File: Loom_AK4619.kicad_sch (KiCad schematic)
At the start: 129 parts, among them J1 Conn_01x40, J2 Conn_01x40, U1 AK4619VN, U101 HT75xx-1-SOT89, U2 AK4619VN, U3 OPA1679, U4 OPA1679, U5 OPA1679, U6 OPA1679

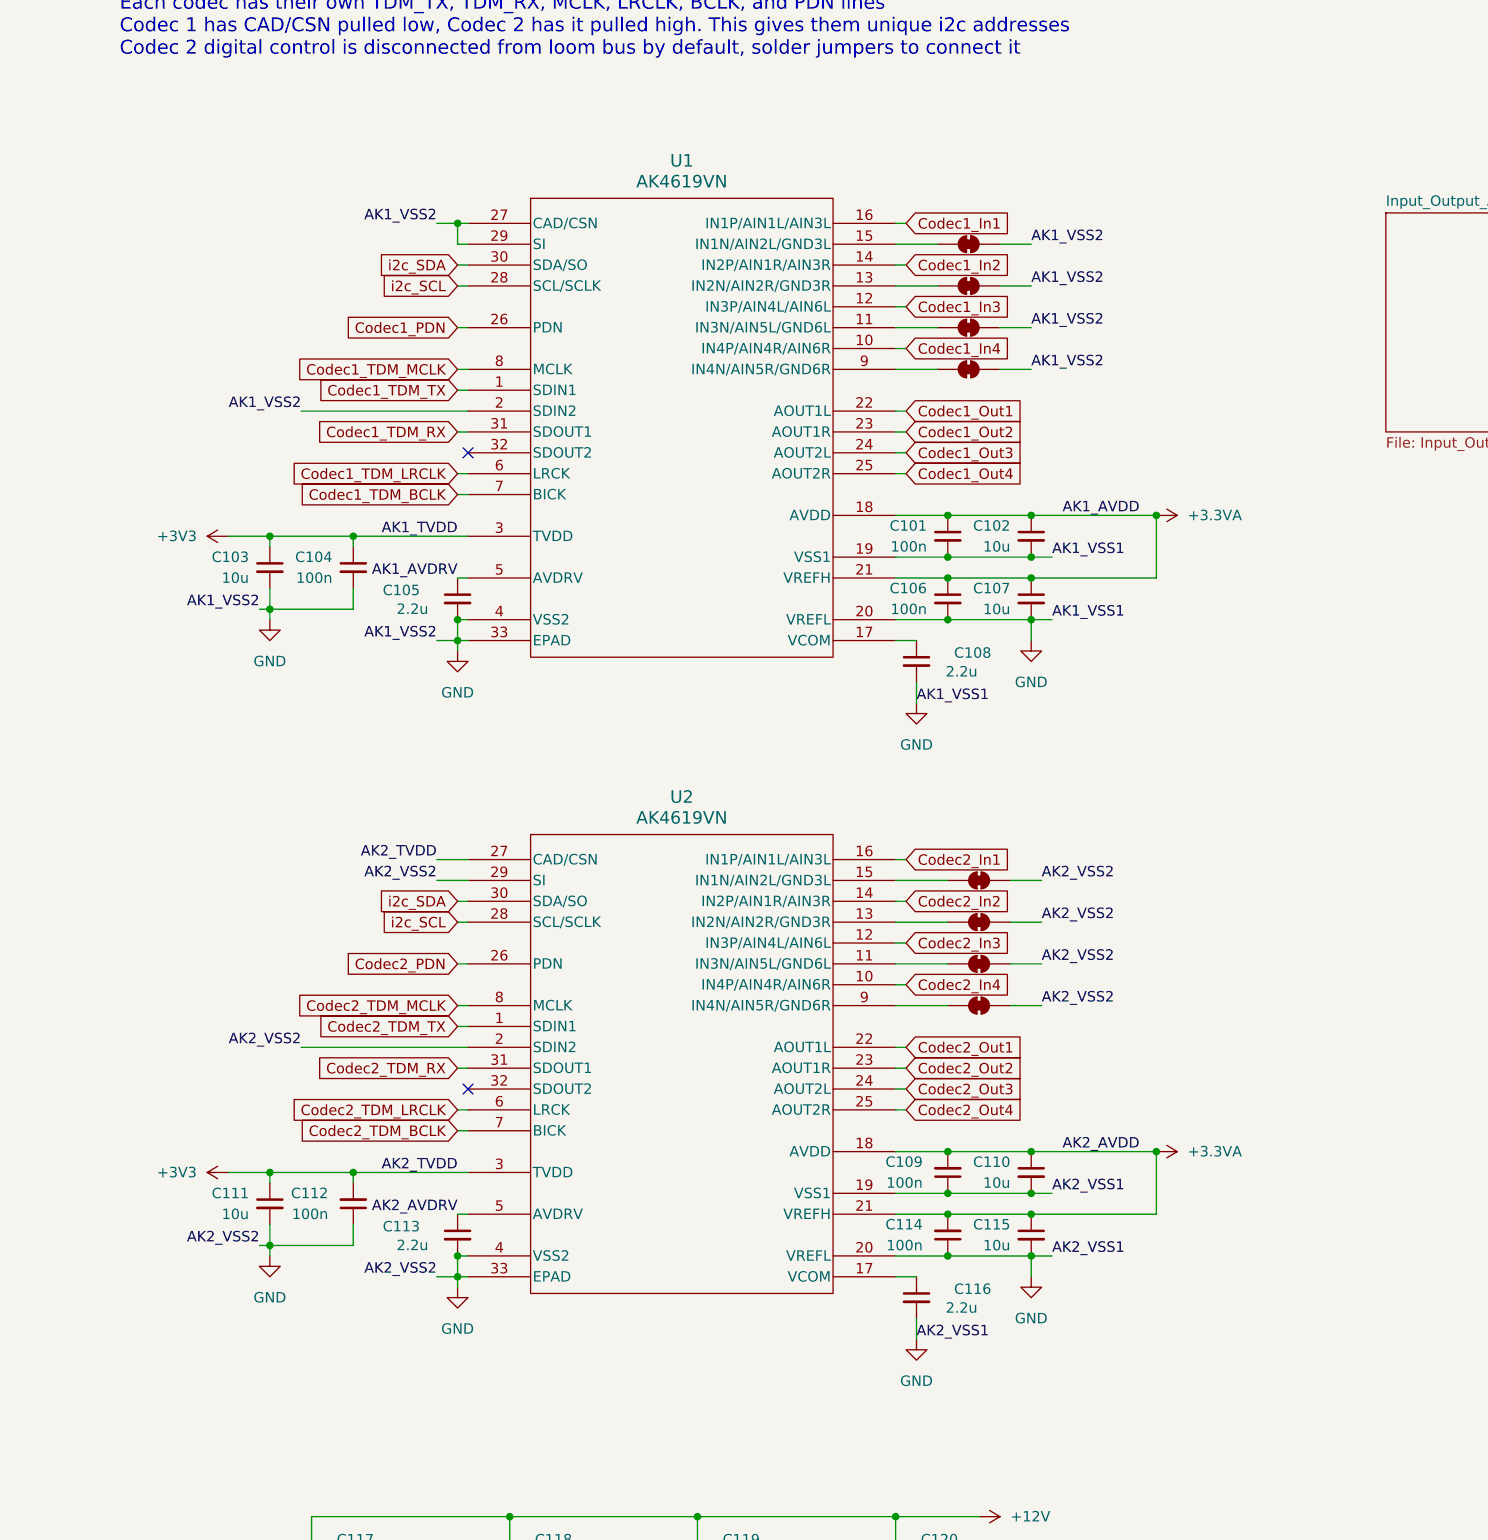
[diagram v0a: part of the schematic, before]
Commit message: Added 33R resistors to SDOUT
Added 33R resistors to SDOUT to decrease slew rate slightly to reduce radiated emissions.
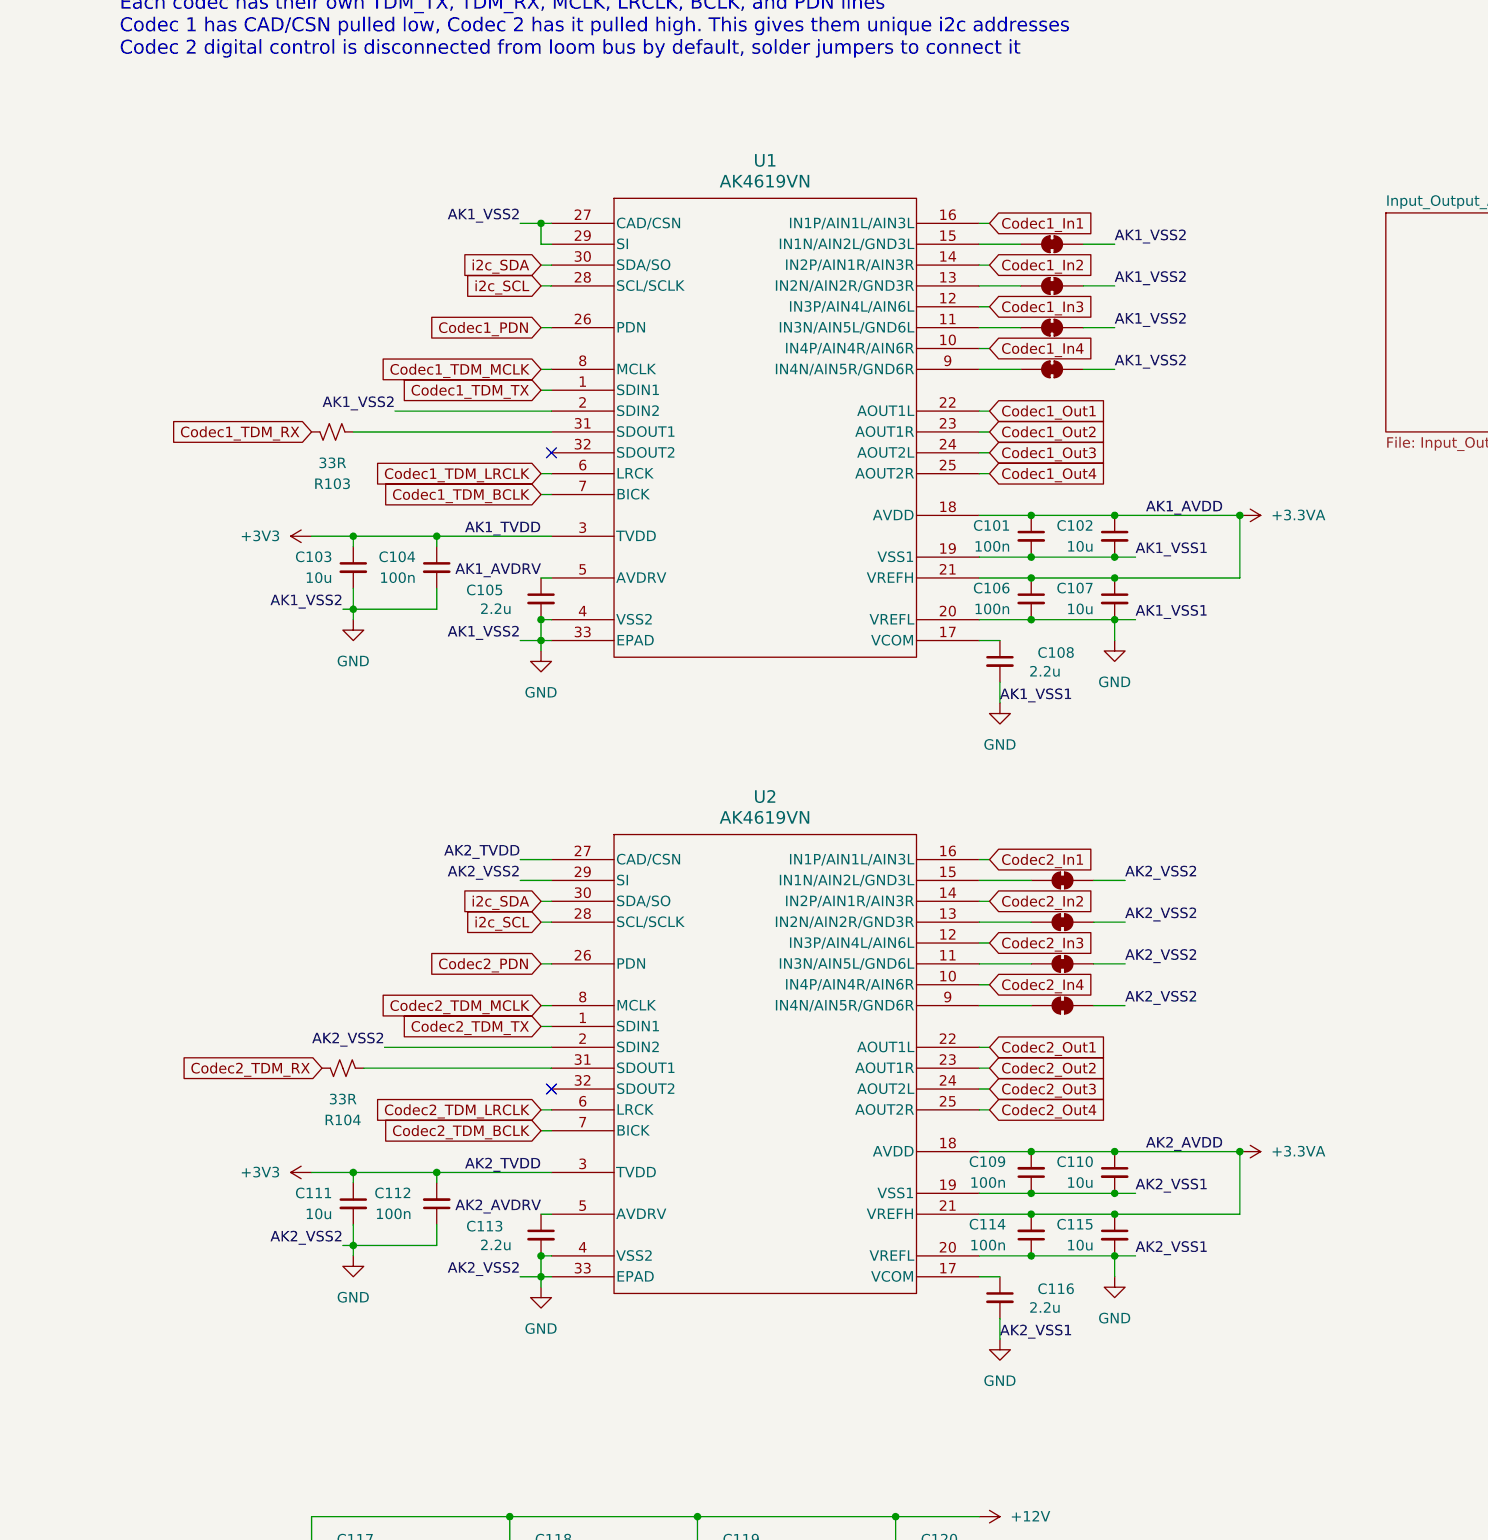
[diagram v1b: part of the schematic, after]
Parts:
- added R103, R104: 33R, winterbloom:R_0603_HandSolder, symbol Decapod_Devices:R_Small_US
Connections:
- net Codec1_TDM_RX: now also R103.1; no longer U1.31 (SDOUT1)
- net Codec2_TDM_RX: now also R104.1; no longer U2.31 (SDOUT1)
- new net: R104.2, U2.31 (SDOUT1)
- new net: R103.2, U1.31 (SDOUT1)
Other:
- moved on the sheet: C101, C102, C103, C104, C105, C106, C107, C108, C109, C110, C111, C112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

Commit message: Version 1 ready to order
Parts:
- R101: LCSC (none) -> C25804
- R102: LCSC (none) -> C23234
- R103, R104: LCSC (none) -> C23140
- U101: LCSC (none) -> C14289
- U3, U4, U5, U6: LCSC (none) -> C2057264
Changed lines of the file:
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@@
 	(label "AK1_VSS2"
 		(at 138.43 64.77 0)
-		(fields_autoplaced yes)
 		(effects
 			(font
@@
 	(label "AK2_VSS2"
 		(at 139.7 147.32 0)
-		(fields_autoplaced yes)
 		(effects
 			(font
@@
 	(label "AK1_VSS2"
 		(at 44.45 109.22 180)
-		(fields_autoplaced yes)
 		(effects
 			(font
@@
 	(label "AK2_TVDD"
 		(at 66.04 139.7 180)
-		(fields_autoplaced yes)
 		(effects
 			(font
@@
 	(label "AK2_VSS2"
 		(at 139.7 152.4 0)
-		(fields_autoplaced yes)
 		(effects
 			(font
@@
 	(label "AK1_VSS2"
 		(at 138.43 69.85 0)
-		(fields_autoplaced yes)
 		(effects
 			(font
@@
 	(label "AK1_TVDD"
 		(at 68.58 100.33 180)
-		(fields_autoplaced yes)
 		(effects
 			(font
@@
 	(label "AK2_VSS2"
 		(at 49.53 162.56 180)
-		(fields_autoplaced yes)
 		(effects
 			(font
@@
 	(label "AK1_AVDRV"
 		(at 68.58 105.41 180)
-		(fields_autoplaced yes)
 		(effects
 			(font
@@
 	(label "AK1_VSS1"
 		(at 140.97 102.87 0)
-		(fields_autoplaced yes)
 		(effects
 			(font
@@
 	(label "AK2_VSS1"
 		(at 140.97 180.34 0)
-		(fields_autoplaced yes)
 		(effects
 			(font
@@
 	(label "AK2_VSS2"
 		(at 66.04 142.24 180)
-		(fields_autoplaced yes)
 		(effects
 			(font
@@
 	(label "AK2_VSS1"
 		(at 140.97 187.96 0)
-		(fields_autoplaced yes)
 		(effects
 			(font
@@
 	(label "AK1_VSS2"
 		(at 66.04 113.03 180)
-		(fields_autoplaced yes)
 		(effects
 			(font
@@
 	(label "AK2_VSS2"
 		(at 139.7 142.24 0)
-		(fields_autoplaced yes)
 		(effects
 			(font
@@
 	(label "AK2_VSS1"
 		(at 124.46 198.12 0)
-		(fields_autoplaced yes)
 		(effects
 			(font
@@
 	(label "AK1_VSS1"
 		(at 140.97 110.49 0)
-		(fields_autoplaced yes)
 		(effects
 			(font
@@
 	(label "AK2_AVDRV"
 		(at 68.58 182.88 180)
-		(fields_autoplaced yes)
 		(effects
 			(font
@@
 	(label "AK1_VSS2"
 		(at 50.8 85.09 180)
-		(fields_autoplaced yes)
 		(effects
 			(font
@@
 	(label "AK2_VSS2"
 		(at 44.45 186.69 180)
-		(fields_autoplaced yes)
 		(effects
 			(font
@@
 	(label "AK1_VSS2"
 		(at 138.43 80.01 0)
-		(fields_autoplaced yes)
 		(effects
 			(font
@@
 	(label "AK2_AVDD"
 		(at 142.24 175.26 0)
-		(fields_autoplaced yes)
 		(effects
 			(font
@@
 	(label "AK1_VSS2"
 		(at 66.04 62.23 180)
-		(fields_autoplaced yes)
 		(effects
 			(font
@@
 	(label "AK2_VSS2"
 		(at 139.7 157.48 0)
-		(fields_autoplaced yes)
 		(effects
 			(font
@@
 	(label "AK1_VSS2"
 		(at 138.43 74.93 0)
-		(fields_autoplaced yes)
 		(effects
 			(font
@@
 	(label "AK1_VSS1"
 		(at 124.46 120.65 0)
-		(fields_autoplaced yes)
 		(effects
 			(font
@@
 	(label "AK2_VSS2"
 		(at 66.04 190.5 180)
-		(fields_autoplaced yes)
 		(effects
 			(font
@@
 	(label "AK1_AVDD"
 		(at 142.24 97.79 0)
-		(fields_autoplaced yes)
 		(effects
 			(font
@@
 	(label "AK2_TVDD"
 		(at 68.58 177.8 180)
-		(fields_autoplaced yes)
 		(effects
 			(font
@@
 			)
 		)
+		(property "LCSC" "C2057264"
+			(at 111.76 238.76 0)
+			(effects
+				(font
+					(size 1.27 1.27)
+				)
+				(hide yes)
+			)
+		)
 		(pin "1"
 		)
@@
 			)
 		)
+		(property "LCSC" "C23140"
+			(at 44.45 165.1 0)
+			(effects
+				(font
+					(size 1.27 1.27)
+				)
+				(hide yes)
+			)
+		)
 		(pin "1"
 		)
@@
 			)
 		)
+		(property "LCSC" "C2057264"
+			(at 64.77 238.76 0)
+			(effects
+				(font
+					(size 1.27 1.27)
+				)
+				(hide yes)
+			)
+		)
 		(pin "1"
 		)
@@
 			)
 		)
+		(property "LCSC" "C2057264"
+			(at 87.63 238.76 0)
+			(effects
+				(font
+					(size 1.27 1.27)
+				)
+				(hide yes)
+			)
+		)
 		(pin "1"
 		)
@@
 			)
 		)
+		(property "LCSC" "C14289"
+			(at 171.45 238.76 0)
+			(effects
+				(font
+					(size 1.27 1.27)
+				)
+				(hide yes)
+			)
+		)
 		(pin "1"
 		)
@@
 			)
 		)
+		(property "LCSC" "C23234"
+			(at 237.49 240.03 0)
+			(effects
+				(font
+					(size 1.27 1.27)
+				)
+				(hide yes)
+			)
+		)
 		(pin "1"
 		)
@@
 			)
 		)
+		(property "LCSC" "C25804"
+			(at 232.41 234.95 0)
+			(effects
+				(font
+					(size 1.27 1.27)
+				)
+				(hide yes)
+			)
+		)
 		(pin "1"
 		)
@@
 			)
 		)
+		(property "LCSC" "C23140"
+			(at 43.18 87.63 0)
+			(effects
+				(font
+					(size 1.27 1.27)
+				)
+				(hide yes)
+			)
+		)
 		(pin "1"
 		)
@@
 			(effects
 				(font
+					(size 1.27 1.27)
+				)
+				(hide yes)
+			)
+		)
+		(property "LCSC" "C2057264"
+			(at 40.64 238.76 0)
+			(effects
+				(font
